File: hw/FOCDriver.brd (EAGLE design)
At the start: 99.1 x 62.3 mm, 119 parts, among them Q1 BC817, Q2 BC817, Q3 BC817, Q4 BC817, Q5 BC817, Q6 BC817, U1 SN74LVC2G17, U10 LMV321SQ3T2G, U11 LMV321SQ3T2G, U2 AO4606, U3 BA7805FP, U4 SN74LVC2G17, U5 AO4606, U6 SN74LVC2G17, U7 AO4606, U8 LMV321SQ3T2G, U9 LMV321SQ3T2G

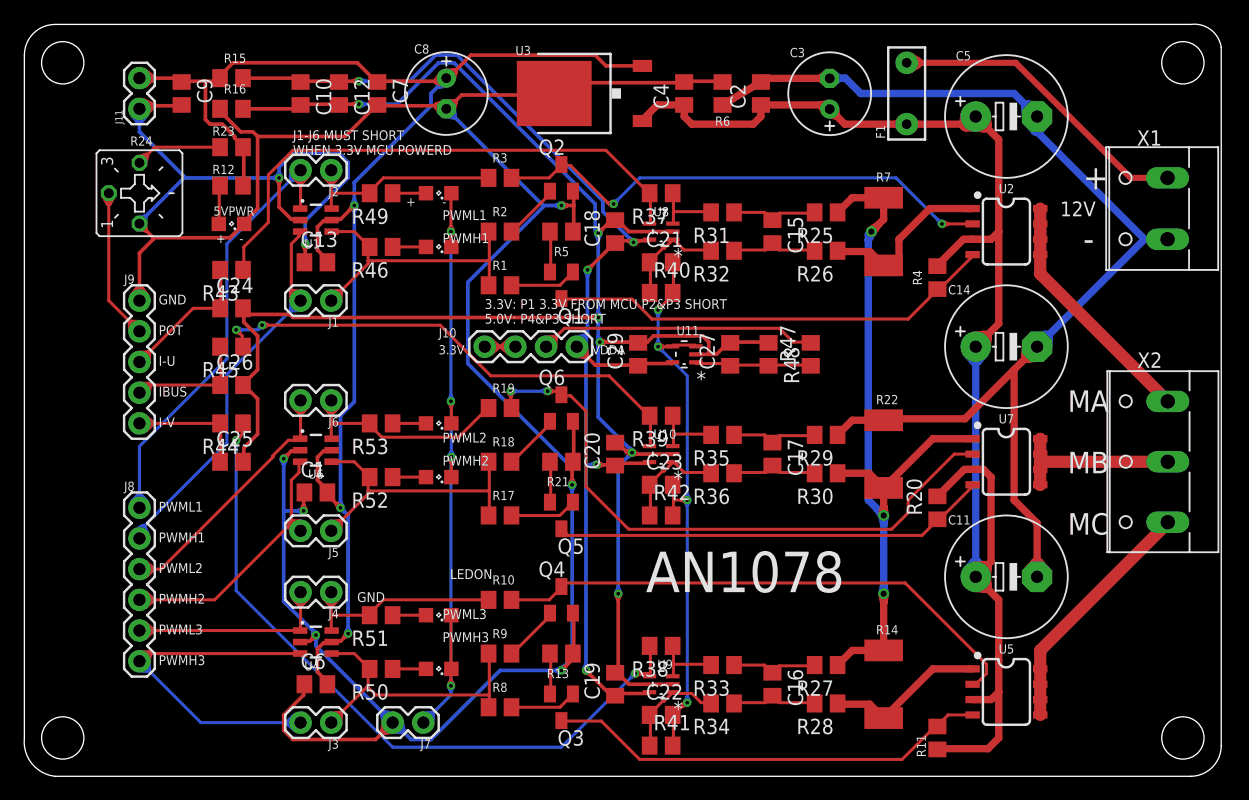
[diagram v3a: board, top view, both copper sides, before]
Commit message: fix layout bugs
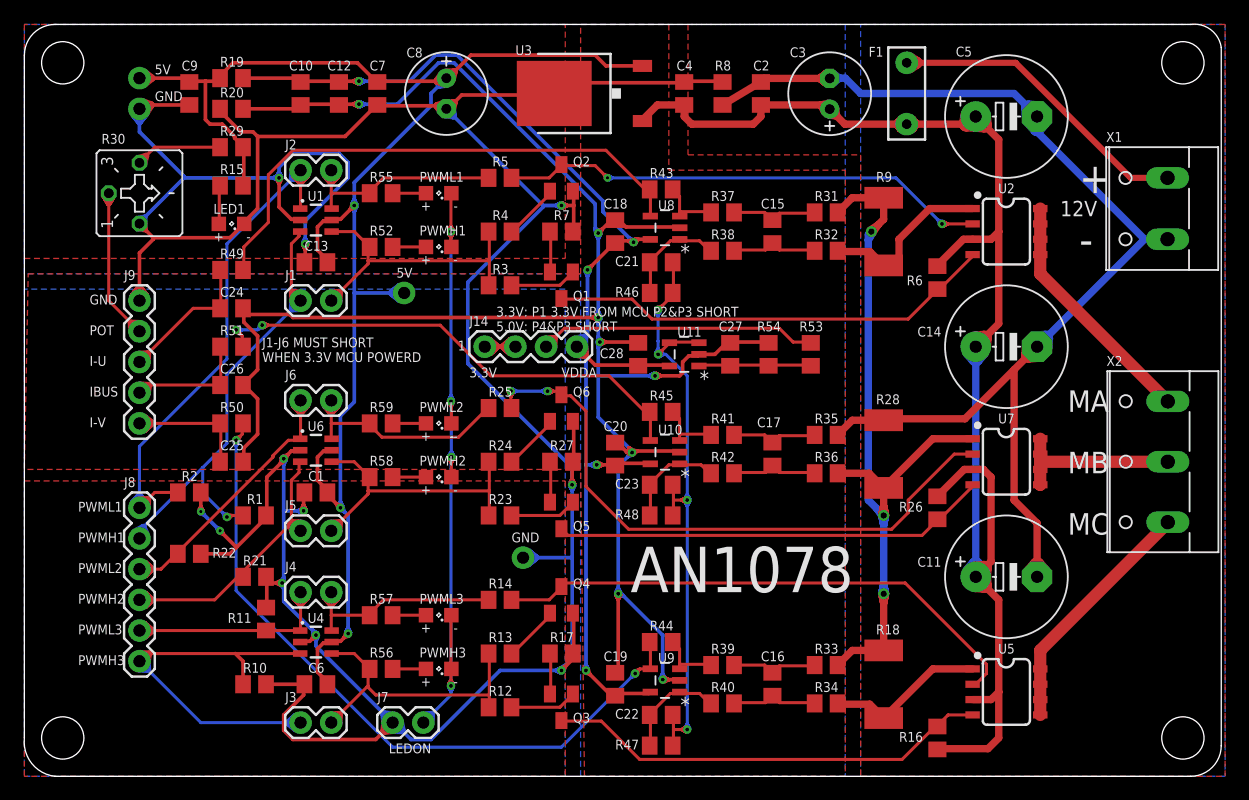
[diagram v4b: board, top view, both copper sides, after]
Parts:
- added J12, J13: (no value), SparkFun-Connectors:1X01_NO_SILK
- added J14: (no value), SparkFun-Connectors:1X04
- added R54: 20K, rcl:R0805
- added R55, R56, R57, R58, R59: 330, rcl:R0805
- C1, C10, C12, C13, C6, C7, C9: value 100n -> 0.1u
- J10: device SparkFun-Connectors:1X04 -> SparkFun-Connectors:1X01_NO_SILK
- J11: device SparkFun-Connectors:1X02 -> SparkFun-Connectors:1X01_NO_SILK
- R1, R10, R2: value 1K -> 4.7K
- R11: value 330 -> 4.7K
- R12, R4, R49, R50, R51: value 330 -> 1K
- R13, R5: value 180 -> 1K
- R14: value 0.025R 2W 1% -> 1K; device resistor:R2512 -> rcl:R0805
- R15, R16, R6: value 0 -> 330
- R17, R27: value 1K -> 180
- R18, R28, R9: value 1K -> 0.025R 2W 1%; device rcl:R0805 -> resistor:R2512
- R19, R8: value 1K -> 0
- R20: value 330 -> 0
- R21: value 180 -> 4.7K
- R22: value 0.025R 2W 1% -> 4.7K; device resistor:R2512 -> rcl:R0805
- R23: value 5.6K -> 1K
- R24: value 10K -> 1K; device pot:CT6 -> rcl:R0805
- R26: value 1K -> 330
- R29: value 1K -> 5.6K
- R30: value 1K -> 10K; device rcl:R0805 -> pot:CT6
- R37, R38, R39, R40, R41, R42: value 20K -> 1K
- R43, R44, R45: value 1K -> 20K
- R46, R53: value 330 -> 20K
- R7: value 0.025R 2W 1% -> 180; device resistor:R2512 -> rcl:R0805
- U10, U11, U8, U9: value LMV321SQ3T2G -> LMV321IDBVRG4; device LMV321SQ3T2G:SOT65P210X110-5N -> LMV321IDBVRG4:SOT95P285X120-5N
- moved R16 78.3 mm to (75.6, 3.17), turned to 270 degrees
- moved R20 67.1 mm to (17.1, 55.2), turned to 0 degrees
- moved R30 61.4 mm to (9.53, 48.3), turned to 270 degrees
- moved R22 58.1 mm to (13.7, 18.4), turned to 0 degrees
- moved R11 56.4 mm to (20.0, 13.0), turned to 90 degrees
- moved R29 54.7 mm to (17.1, 52.1)
- moved R8 54.0 mm to (57.8, 56.5), turned to 90 degrees
- moved R12 48.6 mm to (39.4, 5.71)
- moved R9 47.2 mm to (71.1, 45.1), turned to 270 degrees
- moved R44 39.9 mm to (52.7, 11.1)
- moved R23 37.7 mm to (39.4, 21.6), turned to 0 degrees
- moved R24 37.2 mm to (39.4, 26.0), turned to 0 degrees
- moved R18 36.7 mm to (71.1, 7.62), turned to 270 degrees
- moved R4 36.4 mm to (39.4, 45.1), turned to 0 degrees
- moved J10 36.2 mm to (9.53, 57.8)
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- renumbered 5VPWR to LED1, C29 to C28
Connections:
- net 3V3FROMMCU: now also J14.1, J14.2; no longer J10.1, J10.2
- net 5V: now also J10.1, J12.1, R15.2, R19.1, R29.1; no longer J11.2, R12.2, R15.1, R23.1
- net AGND: now also R20.2, R54.1; no longer R16.2, R48.1
- net DGND: now also J13.1, R1.1, R10.1, R11.2, R17.1, R2.2, R20.1, R22.2, R27.1, R30.A, R7.1, R8.2; no longer R13.1, R16.1, R24.A, R5.1, R6.2
- net GND: now also R28.2, R35.1, R8.1; no longer R22.2, R29.1, R6.1
- net H1: now also R1.2
- net H1O: now also R3.1, R4.1, R52.2; no longer R1.1, R2.1, R46.2
- net H2: now also R10.2
- net H2O: now also R12.1, R13.1, R56.2; no longer R50.2, R8.1, R9.1
- net H3: now also R21.2
- net H3O: now also R23.1, R24.1, R58.2; no longer R17.1, R18.1, R52.2
- net ICOM: now also R18.1, R28.1, R31.1, R33.1, R36.1, R9.1; no longer R14.1, R22.1, R25.1, R27.1, R30.1, R7.1
- net IMOTORA: now also R49.2; no longer R43.2
- net IMOTORB: now also R50.2; no longer R44.2
- net IMOTORBUS: now also R51.2; no longer R45.2
- net IU: now also R32.1, R9.2; no longer R26.1, R7.2
- net IV: now also R18.2, R34.1; no longer R14.2, R28.1
- net L1: now also R2.1
- net L1O: now also R5.1, R55.2; no longer R3.1, R49.2
- net L2: now also R11.1
- net L2O: now also R14.1, R57.2; no longer R10.1, R51.2
- net L3: now also R22.1
- net L3O: now also R25.1, R59.2; no longer R19.1, R53.2
- net N$10: now also R6.1; no longer R4.1
- net N$11: now also R31.2, R37.1; no longer R25.2, R31.1
- net N$12: now also R32.2, R38.1; no longer R26.2, R32.1
- net N$13: now also R37.2, R43.1; no longer R31.2, R37.1
- net N$14: now also R33.2, R39.1; no longer R27.2, R33.1
- net N$15: now also R38.2, R46.1; no longer R32.2, R40.1
- net N$16: now also R43.2, R49.1; no longer R37.2, R43.1
- net N$17: now also R34.2, R40.1; no longer R28.2, R34.1
- net N$18: now also R53.1, R54.2; no longer R47.1, R48.2
- net N$19: now also R39.2, R44.1; no longer R33.2, R38.1
- net N$20: now also R40.2, R47.1; no longer R34.2, R41.1
- net N$21: now also R44.2, R50.1; no longer R38.2, R44.1
- net N$22: now also R35.2, R41.1; no longer R29.2, R35.1
- net N$23: now also R36.2, R42.1; no longer R30.2, R36.1
- net N$24: now also R41.2, R45.1; no longer R35.2, R39.1
- net N$25: now also R42.2, R48.1; no longer R36.2, R42.1
- net N$26: now also R45.2, R51.1; no longer R39.2, R45.1
- net N$28: now also R27.2; no longer R21.2
- net N$3: now also R25.2; no longer R19.2
- net N$30: now also R3.2; no longer R1.2
- net N$31: now also R15.1; no longer R12.1
- net N$32: now also R4.2; no longer R2.2
- net N$33: now also R52.1; no longer R46.1
- net N$34: now also R55.1; no longer R49.1
- net N$35: now also R56.1; no longer R50.1
- net N$36: now also R57.1; no longer R51.1
- net N$37: now also R58.1; no longer R52.1
- net N$38: now also R59.1; no longer R53.1
- net N$39: now also R12.2; no longer R8.2
- net N$4: now also R29.2, R30.E; no longer R23.2, R24.E
- net N$40: now also R7.2; no longer R5.2
- net N$41: now also R13.2; no longer R9.2
- net N$42: now also R23.2; no longer R17.2
- net N$43: now also R17.2; no longer R13.2
- net N$44: now also R24.2; no longer R18.2
- net N$6: now also R26.1; no longer R20.1
- net N$7: now also R14.2; no longer R10.2
- net N$8: now also R16.1; no longer R11.1
- net N$9: now also R5.2; no longer R3.2
- net POT: now also R30.S; no longer R24.S
- net PWRDIV: now also J14.3, R53.2; no longer J10.3, R47.2
- net VDDA: now also J14.4, R19.2; no longer J10.4, R15.2
- net VIN: now also R16.2, R26.2, R6.2; no longer R11.2, R20.2, R4.2
- net VREF: now also R46.2, R47.2, R48.2; no longer R40.2, R41.2, R42.2
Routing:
- net DGND: track 351.6 -> 453.6 mm, vias 8 -> 11
- net AGND: track 200.6 -> 255.6 mm, vias 6 -> 8
- net LEDON: track 104.6 -> 142.7 mm
- net ICOM: track 75.5 -> 100.6 mm
- net VREF: track 78.2 -> 99.7 mm
- net VIN: track 143.1 -> 164.2 mm
- net L1: track 54.0 -> 74.5 mm
- net 5V: track 159.2 -> 176.2 mm
- net VDDA: track 136.6 -> 152.6 mm
- net L3: track 35.5 -> 50.2 mm
- net L2: track 31.0 -> 45.7 mm
- net 3V3FROMMCU: track 17.0 -> 30.9 mm
- net GND: track 112.7 -> 122.9 mm
- net H2: track 42.0 -> 51.3 mm
- net H1: track 40.2 -> 49.0 mm, vias 0 -> 1
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- added copper zone on layer 1, net AGND
- added copper zone on layer 16, net AGND
- added copper zone on layer 1, net DGND
- added copper zone on layer 16, net DGND
- added copper zone on layer 1, net GND
- added copper zone on layer 16, net GND
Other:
- board text added: "1"
- board text added: "5V"

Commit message: fix layout errors
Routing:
- net LEDON: track 142.7 -> 111.3 mm, vias 5 -> 4
- net DGND: track 453.6 -> 467.4 mm
- net 5V: track 176.2 -> 189.0 mm
- net VREF: track 99.7 -> 103.7 mm
- net VIN: track 164.2 -> 167.4 mm
- net L3: track 50.2 -> 53.1 mm
- net L2: track 45.7 -> 48.5 mm
- net AGND: track 255.6 -> 258.5 mm
- net N$3: track 73.1 -> 75.3 mm
- net L1: track 74.5 -> 76.6 mm
- net 3V3FROMMCU: track 30.9 -> 33.1 mm
- net IMOTORB: track 24.5 -> 25.9 mm
- net H3: track 42.3 -> 43.7 mm
- net L1O: track 31.4 -> 32.9 mm
- net L2O: track 31.4 -> 32.9 mm
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
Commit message: normal fix
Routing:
- net VIN: track 167.4 -> 172.5 mm
- net 5V: track 189.0 -> 193.2 mm
- net DGND: track 467.4 -> 470.5 mm
- net L3: track 53.1 -> 50.2 mm
- net L2: track 48.5 -> 45.7 mm
- net LEDON: track 111.3 -> 108.8 mm
- net N$3: track 75.3 -> 73.1 mm
- net L1: track 76.6 -> 74.5 mm
- net 3V3FROMMCU: track 33.1 -> 30.9 mm
- net N$9: track 52.8 -> 54.9 mm
- net VDDA: track 153.2 -> 151.4 mm
- net VREF: track 103.7 -> 105.2 mm
- net IMOTORB: track 25.9 -> 24.5 mm
- net H3: track 43.7 -> 42.3 mm
- net L1O: track 32.9 -> 31.4 mm
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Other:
- board text added: "VREF"
- board text removed: "VDDA"

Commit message: gerber for product
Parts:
- J10: device SparkFun-Connectors:1X01_NO_SILK -> SparkFun-Connectors:1X04
- J14: device SparkFun-Connectors:1X04 -> SparkFun-Connectors:1X01_NO_SILK
- moved J10 36.2 mm to (38.1, 35.6)
- moved J12 26.7 mm to (9.53, 55.2)
- moved J13 24.0 mm to (31.4, 40.0)
- moved J14 17.7 mm to (41.3, 18.1)
- moved J11 2.54 mm to (9.53, 57.8)
- moved F1 1.27 mm to (73.0, 55.2)
- moved R8 0.95 mm to (57.8, 57.5), turned to 180 degrees
- moved C2 0.32 mm to (61.3, 56.5)
- moved C4 0.32 mm to (54.3, 56.5)
- renumbered LED1 to 5VPWR
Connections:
- net 3V3FROMMCU: now also J10.1, J10.2; no longer J14.1, J14.2
- net 5V: now also J11.1, J13.1; no longer J10.1, J12.1
- net DGND: now also J12.1, J14.1; no longer J11.1, J13.1
- net PWRDIV: now also J10.3; no longer J14.3
- net VDDA: now also J10.4; no longer J14.4
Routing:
- net VIN: track 172.5 -> 145.7 mm
- net GND: track 122.5 -> 112.8 mm, vias 0 -> 15
- net DGND: track 470.5 -> 475.4 mm, vias 11 -> 16
- net 5V: track 193.2 -> 197.9 mm
- net N$9: track 54.9 -> 58.2 mm
- net ICOM: track 100.5 -> 97.5 mm
- net N$7: track 45.0 -> 46.7 mm
- net VREF: track 105.2 -> 106.4 mm
- net N$3: track 73.1 -> 74.2 mm
- net N$6: track 36.3 -> 37.1 mm
- net N$10: track 37.2 -> 38.1 mm
- net N$8: track 37.2 -> 37.9 mm
- net AGND: vias 8 -> 13
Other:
- board text added: "V2"
- board text removed: "3.3V: P1 3.3V FROM MCU P2&P3 SHORT 5.0V: P4&P3 SHORT"
